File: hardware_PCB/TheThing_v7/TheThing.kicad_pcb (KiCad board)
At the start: 2 copper layers, 75.2 x 96.6 mm, 178 parts, among them J1 Conn_I2C, J10 Conn_01x03, J11 Conn_01x03, J12 Conn_01x03, J13 Conn_01x03, J14 Conn_01x03, J15 HC-SR04, J16 Conn_01x10, J17 Conn_01x10, J18 Conn_01x15, J19 Conn_01x15, J2 Conn_I2C, J20 D2, J21 D3, J22 D4, J23 D5, J24 D6, J25 D7, J26 D8, J27 D9, J28 D10, J29 D11, J3 Conn_01x03, J30 D12, J31 D13, J32 RST1, J33 RST1, J34 D0, J35 D1, J36 A7, J37 A6, J38 A5, J39 A4, J4 Conn_01x03, J40 A3, J41 A2, J42 A1, J43 A0, J44 AREF, J45 VIN, J46 5V, J47 3V3, J48 GND1, J49 GND2, J5 Conn_01x03, J6 Conn_01x03, J7 Conn_01x03, J8 Conn_01x03, J9 Conn_01x03, Q1 PN2222ABU, SW1 ON, SW2 ON, SW3 ON

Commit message: v7 prototype files for PCB and enclosure
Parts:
- removed the kibuzzard-6640C3B8 at (47.0, 75.0)
- removed kibuzzard-681D1A75: G***, kibuzzard-681D1A75
- removed kibuzzard-681D1A7E: G***, kibuzzard-681D1A7E
- added kibuzzard-6821B0F3: G***, kibuzzard-6821B0F3, F.Cu at (62.4, 45.1)
- added kibuzzard-6821B0FA: G***, kibuzzard-6821B0FA, F.Cu at (72.6, 45.1)
- added kibuzzard-68220AD1: G***, kibuzzard-68220AD1, F.Cu at (48.1, 72.0)
- R13, R14, R15, R16, R17: value 22k -> 20k
- R7: value 1k -> 100E
- moved H2 23.6 mm to (102.5, 69.0)
- moved H1 16.1 mm to (102.5, 65.0)
- moved kibuzzard-681D9A41 12.6 mm to (79.9, 46.2)
- moved kibuzzard-66412AF8 12.5 mm to (96.0, 66.0)
- moved G*** 10.7 mm to (46.9, 54.6)
- moved G*** 7.20 mm to (46.8, 54.5)
- moved kibuzzard-681D1419 5.35 mm to (41.0, 87.8)
- moved kibuzzard-67A22DCA 5.30 mm to (41.3, 130.8)
- moved kibuzzard-67A20268 4.85 mm to (41.0, 87.6)
- moved J11 3.90 mm to (44.8, 80.6)
- moved J12 3.90 mm to (42.3, 80.6)
- moved J13 3.90 mm to (39.7, 80.6)
- moved J14 3.90 mm to (37.2, 80.6)
- moved kibuzzard-681CED7D 3.60 mm to (47.0, 83.5)
- moved kibuzzard-681D0124 3.41 mm to (47.0, 83.7)
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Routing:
- net /SCK: track 47.5 -> 40.9 mm, vias 1 -> 0
- net GND: track 225.7 -> 222.2 mm
- net /8V3: track 10.1 -> 12.2 mm
- net /3V3: track 43.7 -> 45.7 mm
- net /A3: track 45.6 -> 47.6 mm
- net /A2: track 45.5 -> 47.1 mm
- net /SDA: track 76.1 -> 77.7 mm
- net /SCL: track 74.2 -> 75.8 mm
- net A1: track 68.3 -> 69.5 mm
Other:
- board size 75.2 x 96.6 mm -> 80 x 96.6 mm

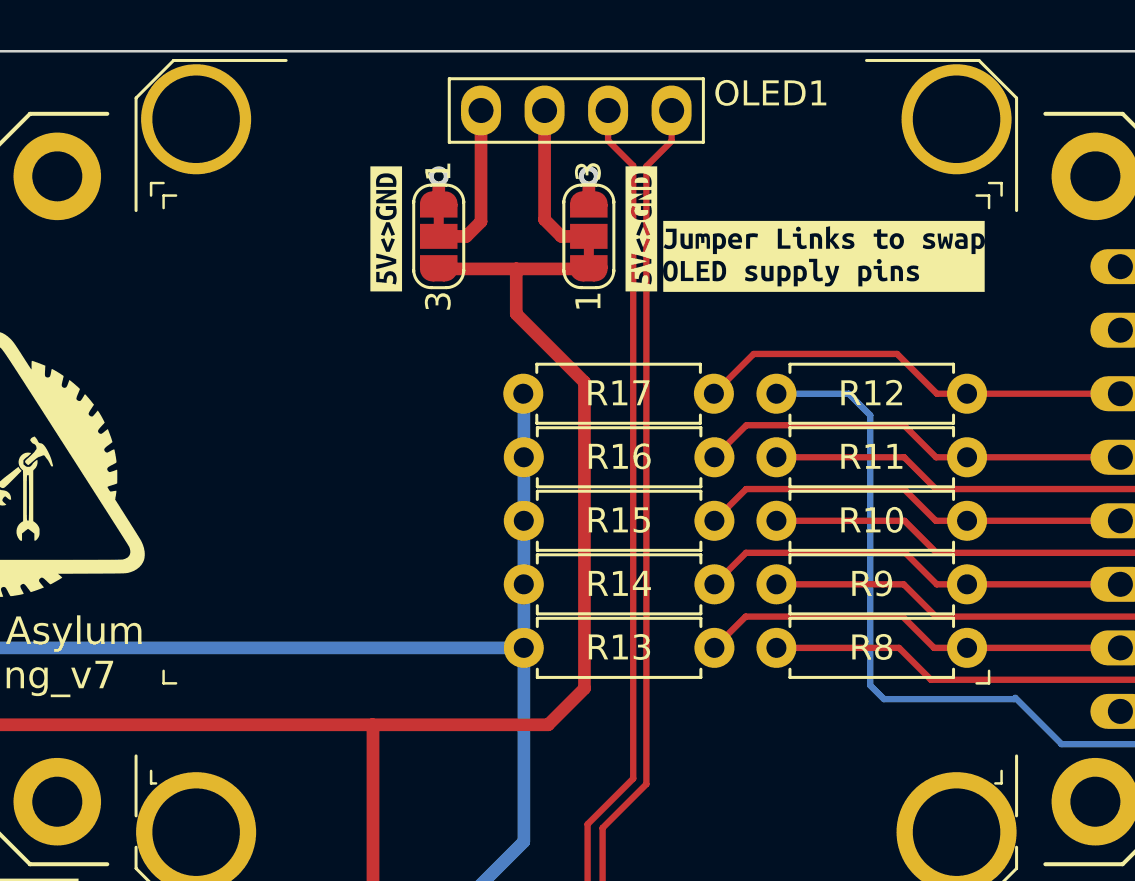
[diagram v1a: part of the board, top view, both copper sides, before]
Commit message: fixed default OLED jumper connections
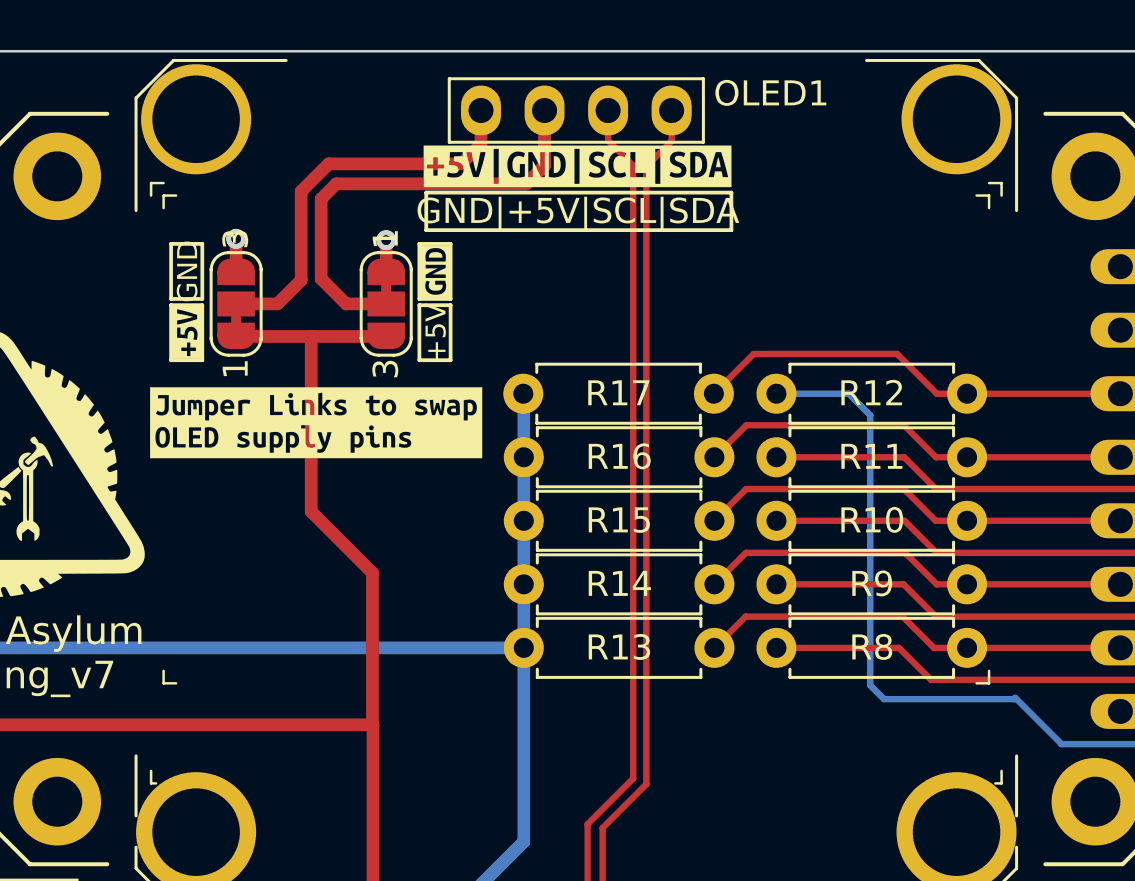
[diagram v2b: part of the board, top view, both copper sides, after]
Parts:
- removed kibuzzard-681D9A41: G***, kibuzzard-681D9A41
- removed kibuzzard-6821B0F3: G***, kibuzzard-6821B0F3
- removed kibuzzard-6821B0FA: G***, kibuzzard-6821B0FA
- added kibuzzard-6827114F: G***, kibuzzard-6827114F, F.Cu at (64.4, 46.8)
- added kibuzzard-682711E3: G***, kibuzzard-682711E3, F.Cu at (54.5, 49.2)
- added kibuzzard-682712AE: G***, kibuzzard-682712AE, F.Cu at (70.0, 42.6)
- added kibuzzard-68271661: G***, kibuzzard-68271661, F.Cu at (59.6, 52.9)
- moved NT5 8.54 mm to (56.4, 48.1), turned to 90 degrees
- moved NT6 8.54 mm to (62.4, 48.1), turned to -90 degrees
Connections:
- NT5 pad 1: GND -> 5V
- NT5 pad 2: /GND_OLED -> /5V_OLED
- NT5 pad 3: 5V -> GND
- NT6 pad 1: 5V -> GND
- NT6 pad 2: /5V_OLED -> /GND_OLED
- NT6 pad 3: GND -> 5V
- OLED1 pad 1: /GND_OLED -> /5V_OLED
- OLED1 pad 2: /5V_OLED -> /GND_OLED
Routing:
- net /GND_OLED: track 6.38 -> 17.9 mm
- net 5V: track 209.8 -> 199.4 mm
- net /5V_OLED: track 6.41 -> 15.9 mm
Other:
- board text added: "+5V"
- board text added: "GND"
- board text added: "GND|+5V|SCL|SDA"
